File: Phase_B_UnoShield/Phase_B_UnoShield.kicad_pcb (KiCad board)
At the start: 2 copper layers, 98.4 x 83.8 mm, 51 parts, among them J1 USB_B_Mini, J3 AVR-ISP-6, J4 ESP_Conn, U1 CA56-12EWA, U2 74HC595, U3 ATmega32U4-A, U4 USBLC6-2SC6, U5 LP2985-3.3, Y1 16MHz

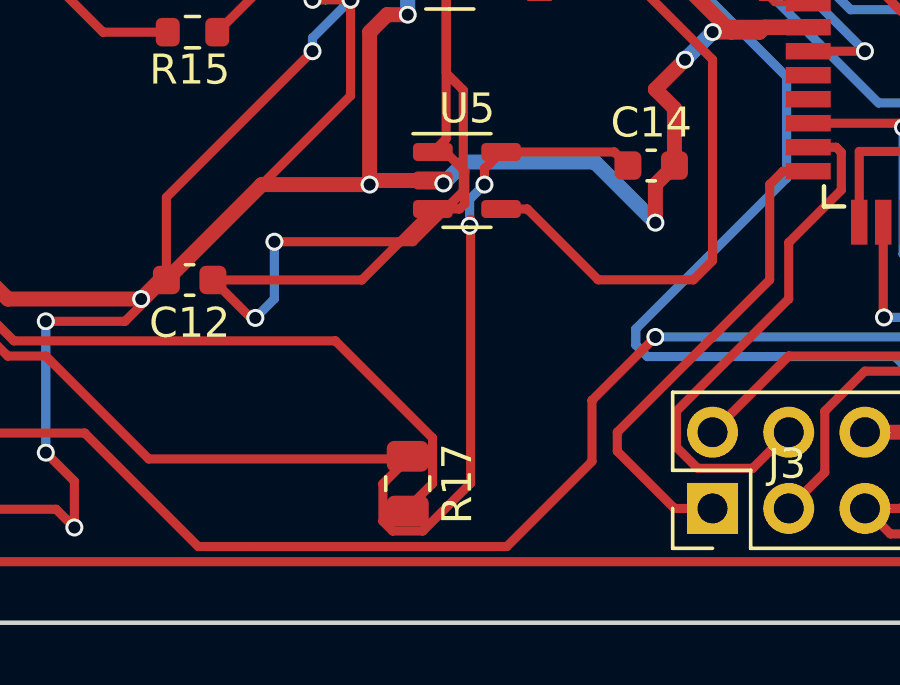
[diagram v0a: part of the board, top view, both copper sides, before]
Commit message: made edits
cause of clearance violations
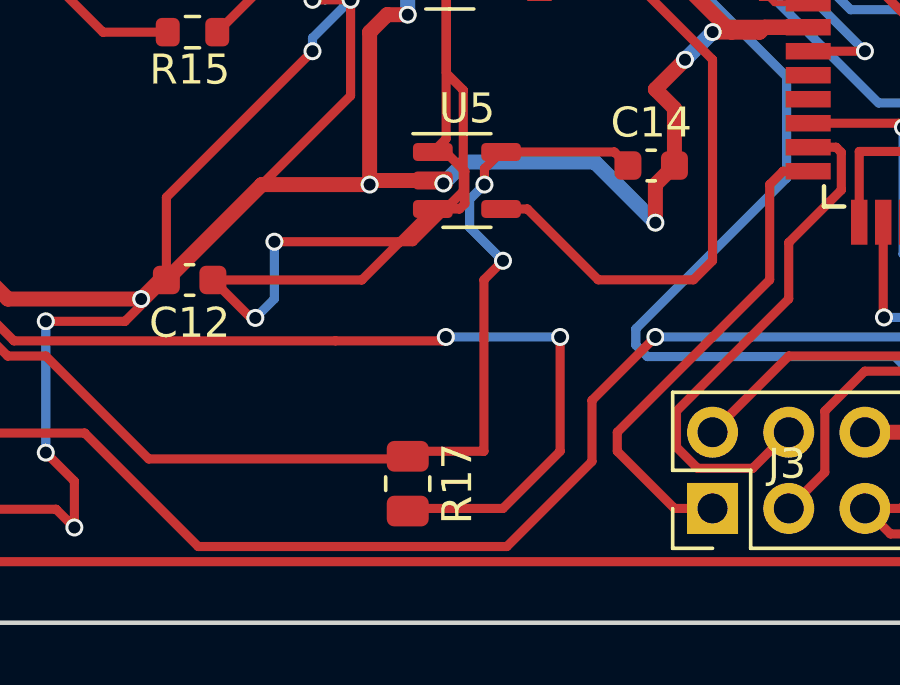
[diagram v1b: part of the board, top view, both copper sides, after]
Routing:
- net Net-(J4-Pin_5): track 39.1 -> 49.0 mm, vias 0 -> 2
- net +3.3V: track 51.4 -> 47.0 mm
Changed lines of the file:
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@@
   (segment (start 33.02 116.84) (end 31.115 114.935) (width 0.305) (layer "F.Cu") (net 44))
   (segment (start 53.244174 110.039174) (end 53.695 110.49) (width 0.305) (layer "F.Cu") (net 44))
+  (segment (start 48.895 114.3) (end 48.895 120.015) (width 0.305) (layer "F.Cu") (net 44))
   (segment (start 26.629549 119.407651) (end 27.804549 118.232651) (width 0.25) (layer "F.Cu") (net 44))
   (segment (start 24.089549 119.407651) (end 26.629549 119.407651) (width 0.305) (layer "F.Cu") (net 44))
   (segment (start 48.912 111.125) (end 48.912 110.593886) (width 0.305) (layer "F.Cu") (net 44))
   (segment (start 21.549549 119.407651) (end 24.089549 119.407651) (width 0.305) (layer "F.Cu") (net 44))
-  (segment (start 46.355 120.27) (end 45.5275 121.0975) (width 0.305) (layer "F.Cu") (net 44))
-  (segment (start 48.451712 112.282466) (end 48.451712 112.532284) (width 0.305) (layer "F.Cu") (net 44))
   (segment (start 31.115 114.935) (end 31.1022 114.935) (width 0.305) (layer "F.Cu") (net 44))
   (segment (start 37.72 120.27) (end 34.29 116.84) (width 0.305) (layer "F.Cu") (net 44))
-  (segment (start 45.851147 122.6725) (end 46.858853 122.6725) (width 0.305) (layer "F.Cu") (net 44))
-  (segment (start 45.5275 122.348853) (end 45.851147 122.6725) (width 0.305) (layer "F.Cu") (net 44))
   (segment (start 48.912 110.593886) (end 49.466712 110.039174) (width 0.305) (layer "F.Cu") (net 44))
-  (segment (start 48.451712 121.079641) (end 48.451712 112.282466) (width 0.305) (layer "F.Cu") (net 44))
-  (segment (start 45.5275 121.0975) (end 45.5275 122.348853) (width 0.305) (layer "F.Cu") (net 44))
   (segment (start 46.355 120.27) (end 37.72 120.27) (width 0.305) (layer "F.Cu") (net 44))
-  (segment (start 46.858853 122.6725) (end 48.451712 121.079641) (width 0.305) (layer "F.Cu") (net 44))
-  (segment (start 48.451712 112.532284) (end 48.417158 112.49773) (width 0.305) (layer "F.Cu") (net 44))
   (segment (start 49.466712 110.039174) (end 53.244174 110.039174) (width 0.305) (layer "F.Cu") (net 44))
+  (segment (start 49.53 113.665) (end 48.895 114.3) (width 0.305) (layer "F.Cu") (net 44))
+  (segment (start 46.5225 120.015) (end 46.355 120.1825) (width 0.305) (layer "F.Cu") (net 44))
   (segment (start 27.804549 118.232651) (end 31.1022 114.935) (width 0.25) (layer "F.Cu") (net 44))
+  (segment (start 48.895 120.015) (end 46.5225 120.015) (width 0.305) (layer "F.Cu") (net 44))
   (segment (start 34.29 116.84) (end 33.02 116.84) (width 0.305) (layer "F.Cu") (net 44))
-  (via (at 48.417158 112.49773) (size 0.6) (drill 0.4) (layers "F.Cu" "B.Cu") (net 44))
+  (via (at 49.53 113.665) (size 0.6) (drill 0.4) (layers "F.Cu" "B.Cu") (net 44))
   (via (at 48.912 111.125) (size 0.6) (drill 0.4) (layers "F.Cu" "B.Cu") (net 44))
-  (segment (start 48.417158 111.619842) (end 48.912 111.125) (width 0.305) (layer "B.Cu") (net 44))
-  (segment (start 48.417158 112.49773) (end 48.417158 111.619842) (width 0.305) (layer "B.Cu") (net 44))
+  (segment (start 48.417158 112.552158) (end 49.53 113.665) (width 0.305) (layer "B.Cu") (net 44))
+  (segment (start 48.912 111.125) (end 48.417158 111.619842) (width 0.305) (layer "B.Cu") (net 44))
+  (segment (start 48.417158 111.619842) (end 48.417158 112.552158) (width 0.305) (layer "B.Cu") (net 44))
   (segment (start 26.135 103.335) (end 32.555 103.335) (width 0.305) (layer "F.Cu") (net 47))
   (segment (start 35.56 100.33) (end 37.590001 100.33) (width 0.305) (layer "F.Cu") (net 47))
@@
   (via (at 54.61 116.205) (size 0.6) (drill 0.4) (layers "F.Cu" "B.Cu") (net 52))
   (segment (start 54.61 116.205) (end 67.31 116.205) (width 0.305) (layer "B.Cu") (net 52))
+  (segment (start 43.945 116.335) (end 47.495 116.335) (width 0.305) (layer "F.Cu") (net 54))
   (segment (start 24.826608 114.43) (end 31.324178 114.43) (width 0.305) (layer "F.Cu") (net 54))
   (segment (start 33.229178 116.335) (end 43.945 116.335) (width 0.305) (layer "F.Cu") (net 54))
-  (segment (start 47.1825 119.5725) (end 47.1825 121.0925) (width 0.305) (layer "F.Cu") (net 54))
+  (segment (start 47.495 116.335) (end 47.625 116.205) (width 0.305) (layer "F.Cu") (net 54))
   (segment (start 20.347049 119.905743) (end 20.347049 118.909559) (width 0.305) (layer "F.Cu") (net 54))
   (segment (start 24.089549 121.947651) (end 22.752049 120.610151) (width 0.305) (layer "F.Cu") (net 54))
-  (segment (start 47.1825 121.0925) (end 46.355 121.92) (width 0.305) (layer "F.Cu") (net 54))
-  (segment (start 43.945 116.335) (end 47.1825 119.5725) (width 0.305) (layer "F.Cu") (net 54))
+  (segment (start 49.53 121.92) (end 46.4425 121.92) (width 0.305) (layer "F.Cu") (net 54))
+  (segment (start 51.435 120.015) (end 49.53 121.92) (width 0.305) (layer "F.Cu") (net 54))
+  (segment (start 51.435 116.205) (end 51.435 120.015) (width 0.305) (layer "F.Cu") (net 54))
   (segment (start 20.347049 118.909559) (end 24.826608 114.43) (width 0.305) (layer "F.Cu") (net 54))
   (segment (start 31.324178 114.43) (end 33.229178 116.335) (width 0.305) (layer "F.Cu") (net 54))
   (segment (start 21.051457 120.610151) (end 20.347049 119.905743) (width 0.305) (layer "F.Cu") (net 54))
   (segment (start 22.752049 120.610151) (end 21.051457 120.610151) (width 0.305) (layer "F.Cu") (net 54))
+  (via (at 51.435 116.205) (size 0.6) (drill 0.4) (layers "F.Cu" "B.Cu") (net 54))
+  (via (at 47.625 116.205) (size 0.6) (drill 0.4) (layers "F.Cu" "B.Cu") (net 54))
+  (segment (start 47.625 116.205) (end 51.435 116.205) (width 0.305) (layer "B.Cu") (net 54))
   (segment (start 21.549549 121.947651) (end 23.296898 123.695) (width 0.305) (layer "F.Cu") (net 56))
   (segment (start 68.58 114.935) (end 68.605 114.91) (width 0.305) (layer "F.Cu") (net 56))

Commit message: Edit version 2
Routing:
- net Net-(J4-Pin_5): track 49.0 -> 44.3 mm
- net +3.3V: track 47.0 -> 45.1 mm
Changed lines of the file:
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@@
   (segment (start 33.02 116.84) (end 31.115 114.935) (width 0.305) (layer "F.Cu") (net 44))
   (segment (start 53.244174 110.039174) (end 53.695 110.49) (width 0.305) (layer "F.Cu") (net 44))
-  (segment (start 48.895 114.3) (end 48.895 120.015) (width 0.305) (layer "F.Cu") (net 44))
   (segment (start 26.629549 119.407651) (end 27.804549 118.232651) (width 0.25) (layer "F.Cu") (net 44))
   (segment (start 24.089549 119.407651) (end 26.629549 119.407651) (width 0.305) (layer "F.Cu") (net 44))
   (segment (start 48.912 111.125) (end 48.912 110.593886) (width 0.305) (layer "F.Cu") (net 44))
   (segment (start 21.549549 119.407651) (end 24.089549 119.407651) (width 0.305) (layer "F.Cu") (net 44))
+  (segment (start 48.895 114.935) (end 46.99 116.84) (width 0.305) (layer "F.Cu") (net 44))
   (segment (start 31.115 114.935) (end 31.1022 114.935) (width 0.305) (layer "F.Cu") (net 44))
   (segment (start 37.72 120.27) (end 34.29 116.84) (width 0.305) (layer "F.Cu") (net 44))
+  (segment (start 46.99 116.84) (end 46.99 119.5475) (width 0.305) (layer "F.Cu") (net 44))
   (segment (start 48.912 110.593886) (end 49.466712 110.039174) (width 0.305) (layer "F.Cu") (net 44))
   (segment (start 46.355 120.27) (end 37.72 120.27) (width 0.305) (layer "F.Cu") (net 44))
   (segment (start 49.466712 110.039174) (end 53.244174 110.039174) (width 0.305) (layer "F.Cu") (net 44))
-  (segment (start 49.53 113.665) (end 48.895 114.3) (width 0.305) (layer "F.Cu") (net 44))
-  (segment (start 46.5225 120.015) (end 46.355 120.1825) (width 0.305) (layer "F.Cu") (net 44))
+  (segment (start 48.895 113.03) (end 48.895 114.935) (width 0.305) (layer "F.Cu") (net 44))
+  (segment (start 46.99 119.5475) (end 46.355 120.1825) (width 0.305) (layer "F.Cu") (net 44))
   (segment (start 27.804549 118.232651) (end 31.1022 114.935) (width 0.25) (layer "F.Cu") (net 44))
-  (segment (start 48.895 120.015) (end 46.5225 120.015) (width 0.305) (layer "F.Cu") (net 44))
   (segment (start 34.29 116.84) (end 33.02 116.84) (width 0.305) (layer "F.Cu") (net 44))
-  (via (at 49.53 113.665) (size 0.6) (drill 0.4) (layers "F.Cu" "B.Cu") (net 44))
+  (via (at 48.895 113.03) (size 0.6) (drill 0.4) (layers "F.Cu" "B.Cu") (net 44))
   (via (at 48.912 111.125) (size 0.6) (drill 0.4) (layers "F.Cu" "B.Cu") (net 44))
-  (segment (start 48.417158 112.552158) (end 49.53 113.665) (width 0.305) (layer "B.Cu") (net 44))
-  (segment (start 48.912 111.125) (end 48.417158 111.619842) (width 0.305) (layer "B.Cu") (net 44))
   (segment (start 48.417158 111.619842) (end 48.417158 112.552158) (width 0.305) (layer "B.Cu") (net 44))
+  (segment (start 48.417158 111.619842) (end 48.912 111.125) (width 0.305) (layer "B.Cu") (net 44))
+  (segment (start 48.417158 112.552158) (end 48.895 113.03) (width 0.305) (layer "B.Cu") (net 44))
   (segment (start 26.135 103.335) (end 32.555 103.335) (width 0.305) (layer "F.Cu") (net 47))
   (segment (start 35.56 100.33) (end 37.590001 100.33) (width 0.305) (layer "F.Cu") (net 47))
@@
   (via (at 54.61 116.205) (size 0.6) (drill 0.4) (layers "F.Cu" "B.Cu") (net 52))
   (segment (start 54.61 116.205) (end 67.31 116.205) (width 0.305) (layer "B.Cu") (net 52))
-  (segment (start 43.945 116.335) (end 47.495 116.335) (width 0.305) (layer "F.Cu") (net 54))
+  (segment (start 43.815 116.335) (end 45.59 116.335) (width 0.305) (layer "F.Cu") (net 54))
+  (segment (start 33.229178 116.335) (end 43.815 116.335) (width 0.305) (layer "F.Cu") (net 54))
   (segment (start 24.826608 114.43) (end 31.324178 114.43) (width 0.305) (layer "F.Cu") (net 54))
-  (segment (start 33.229178 116.335) (end 43.945 116.335) (width 0.305) (layer "F.Cu") (net 54))
-  (segment (start 47.495 116.335) (end 47.625 116.205) (width 0.305) (layer "F.Cu") (net 54))
   (segment (start 20.347049 119.905743) (end 20.347049 118.909559) (width 0.305) (layer "F.Cu") (net 54))
+  (segment (start 45.59 116.335) (end 45.72 116.205) (width 0.305) (layer "F.Cu") (net 54))
   (segment (start 24.089549 121.947651) (end 22.752049 120.610151) (width 0.305) (layer "F.Cu") (net 54))
-  (segment (start 49.53 121.92) (end 46.4425 121.92) (width 0.305) (layer "F.Cu") (net 54))
-  (segment (start 51.435 120.015) (end 49.53 121.92) (width 0.305) (layer "F.Cu") (net 54))
-  (segment (start 51.435 116.205) (end 51.435 120.015) (width 0.305) (layer "F.Cu") (net 54))
+  (segment (start 48.8075 122.0075) (end 46.355 122.0075) (width 0.305) (layer "F.Cu") (net 54))
+  (segment (start 50.165 120.65) (end 48.8075 122.0075) (width 0.305) (layer "F.Cu") (net 54))
   (segment (start 20.347049 118.909559) (end 24.826608 114.43) (width 0.305) (layer "F.Cu") (net 54))
   (segment (start 31.324178 114.43) (end 33.229178 116.335) (width 0.305) (layer "F.Cu") (net 54))
   (segment (start 21.051457 120.610151) (end 20.347049 119.905743) (width 0.305) (layer "F.Cu") (net 54))
   (segment (start 22.752049 120.610151) (end 21.051457 120.610151) (width 0.305) (layer "F.Cu") (net 54))
-  (via (at 51.435 116.205) (size 0.6) (drill 0.4) (layers "F.Cu" "B.Cu") (net 54))
-  (via (at 47.625 116.205) (size 0.6) (drill 0.4) (layers "F.Cu" "B.Cu") (net 54))
-  (segment (start 47.625 116.205) (end 51.435 116.205) (width 0.305) (layer "B.Cu") (net 54))
+  (via (at 45.72 116.205) (size 0.6) (drill 0.4) (layers "F.Cu" "B.Cu") (net 54))
+  (via (at 50.165 120.65) (size 0.6) (drill 0.4) (layers "F.Cu" "B.Cu") (net 54))
+  (segment (start 45.72 116.205) (end 50.165 120.65) (width 0.305) (layer "B.Cu") (net 54))
   (segment (start 21.549549 121.947651) (end 23.296898 123.695) (width 0.305) (layer "F.Cu") (net 56))
   (segment (start 68.58 114.935) (end 68.605 114.91) (width 0.305) (layer "F.Cu") (net 56))
